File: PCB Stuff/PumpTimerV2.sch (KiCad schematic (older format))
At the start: 16 parts, among them J1 Conn_02x12_Odd_Even, J2 1935161, J3 282856-2, J4 282856-2, K1 ADW1205HLW, K2 ADW1205HLW, Q1 DMN67D7L, Q2 DMN67D7L

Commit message: Delete Altium files, add full Kicad project, update Kicad files
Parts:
- removed BT?: Battery_Cell, symbol Device:Battery_Cell
- removed C?: GMC31X5R107M10NT, Capacitor_SMD:C_1206_3216Metric_Pad1.33x1.80mm_HandSolder, symbol Device:C
- removed J3: 282856-2, TE_282856-2, symbol Connector:282856-2
- added BT1: 2032, Battery:BAT_HLD_2032, symbol Mechanical:Battery_Cell_Holder_2032
- added C1: 100u, Capacitor_SMD:C_1206_3216Metric_Pad1.33x1.80mm_HandSolder, symbol Device:C
- added J2: 282856-2, TE_282856-2, symbol Connector:282856-2
- added J5, J7: B6B-PH-SM4-TBT(LF)(SN), Connector_JST:JST_PH_B6B-PH-SM4-TB_1x06-1MP_P2.00mm_Vertical, symbol Connector_Generic:Conn_01x06
- added J6, J8: B4B-PH-SM4-TBT(LF)(SN), Connector_JST:JST_PH_B4B-PH-SM4-TB_1x04-1MP_P2.00mm_Vertical, symbol Connector_Generic:Conn_01x04
- added R1, R2: 1k, Resistor_SMD:R_0603_1608Metric_Pad0.98x0.95mm_HandSolder, symbol Device:R_US
- added R10, R11, R12, R5, R6, R7, R8, R9: 49.9, Resistor_SMD:R_0603_1608Metric_Pad0.98x0.95mm_HandSolder, symbol Device:R_US
- added R3, R4: 2k2, Resistor_SMD:R_0603_1608Metric_Pad0.98x0.95mm_HandSolder, symbol Device:R_US
- C2: renamed from C?; value GMC31X5R107M10NT -> 100u
- PS1: footprint CONV_RAC03-05SK -> power:RAC03-05SK
- U1: renamed from U?; footprint (none) -> Package_SO:SOP-14_127P780x200
- gave numbers to parts that had none: 1
- renumbered D2 to D3, J2 to J1, J4 to J3, J1 to J4
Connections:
- net labels added: RLY_R, RLY_S, RTC_~INT~
- net labels removed: GPIO14(Tx), GPIO15(Rx), GPIO17, GPIO18, GPIO4(CLK0)
- wire segments 70 -> 117
- no-connect marks 1 -> 4
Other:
- note added: "Expansion Ports\n (just in case)"
- note added: "Power Interface"
- note added: "Raspberry Pi Zero W Interface"
- note added: "Real-Time Clock"
- moved on the sheet: C2, D1, D2, D3, J1, J3, K1, K2, PS1, Q1, Q2, U1

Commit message: Adding button interface + LED indicator for manual switching of pump state
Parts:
- added D?: LED, symbol Device:LED
- added R?: R_US, symbol Device:R_US
- added R?: 2k2, Resistor_SMD:R_0603_1608Metric_Pad0.98x0.95mm_HandSolder, symbol Device:R_US
- added SW?: SW_Push, symbol Switch:SW_Push
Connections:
- net labels added: +3V3, ~BTN_RDY~
- wire segments 117 -> 127
- no-connect marks 4 -> 3
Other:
- moved on the sheet: U1

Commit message: Beginning layout. Removed a few non-critical components that will not fit.
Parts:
- removed J5, J7: B6B-PH-SM4-TBT(LF)(SN), Connector_JST:JST_PH_B6B-PH-SM4-TB_1x06-1MP_P2.00mm_Vertical, symbol Connector_Generic:Conn_01x06
- removed J8: B4B-PH-SM4-TBT(LF)(SN), Connector_JST:JST_PH_B4B-PH-SM4-TB_1x04-1MP_P2.00mm_Vertical, symbol Connector_Generic:Conn_01x04
- removed R12: 49.9, Resistor_SMD:R_0603_1608Metric_Pad0.98x0.95mm_HandSolder, symbol Device:R_US
- D4: renamed from D?; footprint (none) -> LED_SMD:LED_0603_1608Metric_Castellated; Part (none) -> SML-D12U1WT86
- R14: renamed from R?; value R_US -> 330; footprint (none) -> Resistor_SMD:R_0603_1608Metric_Pad0.98x0.95mm_HandSolder; Part (none) -> CRGCQ0603F330R
- SW1: renamed from SW?; value SW_Push -> TL3305AF160QG; footprint (none) -> Button_Switch_SMD:TL3305AF160QG; Part (none) -> TL3305AF160QG
- gave numbers to parts that had none: 1
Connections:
- wire segments 127 -> 108
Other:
- note added: "I2C Expansion Port\n (just in case)"
- note added: "NEED TO CHANGE TO CR1025"
- note added: "Override Button\n and Indicator"
- note removed: "Expansion Ports\n (just in case)"
- moved on the sheet: D1, D3, D4, J6, K1, K2, Q1, Q2, R1, R10, R11, R13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

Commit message: Same as last. Need to flip RPI and connector. Line up for mounting.
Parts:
- BT1: value 2032 -> 1632; footprint Battery:BAT_HLD_2032 -> temp:Vertical_16mm_coin; symbol Mechanical:Battery_Cell_Holder_2032 -> battery_cell:Battery_Cell
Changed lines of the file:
@@
 	9150 5500 9150 5550
 $Comp
-L Mechanical:Battery_Cell_Holder_2032 BT1
+L battery_cell:Battery_Cell BT1
 U 1 1 6076BE04
 P 9150 5400
 F 0 "BT1" H 9268 5496 50  0000 L CNN
-F 1 "2032" H 9268 5405 50  0000 L CNN
-F 2 "Battery:BAT_HLD_2032" V 9150 5460 50  0001 C CNN
+F 1 "1632" H 9268 5405 50  0000 L CNN
+F 2 "temp:Vertical_16mm_coin" V 9150 5460 50  0001 C CNN
 F 3 "~" V 9150 5460 50  0001 C CNN
 	1    9150 5400

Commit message: Clean-up, changing board size + adding bigger header for rpi
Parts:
- BT1: footprint temp:Vertical_16mm_coin -> Battery:Vertical_16mm_coin_holder; Part (none) -> Keystone 1069
- J4: value Conn_02x12_Odd_Even -> Conn_02x20_Odd_Even; footprint Connector_PinHeader_2.54mm:PinHeader_2x12_P2.54mm_Vertical -> Connector_PinHeader_2.54mm:PinHeader_2x20_P2.54mm_Vertical; symbol Connector_Generic:Conn_02x12_Odd_Even -> Connector_Generic:Conn_02x20_Odd_Even
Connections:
- no-connect marks 3 -> 19
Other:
- note removed: "NEED TO CHANGE TO CR1025"
- moved on the sheet: R10, R11, R3, R4, R5, R6, R7, R8, R9

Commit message: Routing and placement
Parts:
- removed R10, R11, R5, R6, R7, R8, R9: 49.9, Resistor_SMD:R_0603_1608Metric_Pad0.98x0.95mm_HandSolder, symbol Device:R_US
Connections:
- net +3V3: no longer R13.1
- net +5VD: now also R13.1
- net RLY_S: now also J4.8 (Pin_8); no longer J4.7 (Pin_7)
- net GPIO25: no longer names the net of J4.22 (Pin_22)
- net GPIO9(MISO): no longer names the net of J4.21 (Pin_21)
- no-connect marks 19 -> 28
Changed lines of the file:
@@
 Text Label 6150 2350 0    50   ~ 0
 RTC_~INT~
-Text Label 5550 2450 0    50   ~ 0
-GPIO27
-Text Label 5550 2550 0    50   ~ 0
-GPIO22
-NoConn ~ 6650 2650
-Wire Wire Line
-	6700 2650 6650 2650
-Text Label 5350 2750 0    50   ~ 0
-GPIO10(MOSI)
-Text Label 5350 2950 0    50   ~ 0
-GPIO11(SCLK)
 Wire Wire Line
 	6050 2250 6700 2250
 Wire Wire Line
 	6700 2350 6150 2350
-Wire Wire Line
-	6700 2850 6150 2850
 $Comp
 L power:GND #PWR023
@@
 	-1   0    0    1
 $EndComp
-Text Label 7800 2550 0    50   ~ 0
-GPIO23
-Text Label 7800 2650 0    50   ~ 0
-GPIO24
 $Comp
 L power:GND #PWR024
@@
 	-1   0    0    1
 $EndComp
-Text Label 7350 2850 0    50   ~ 0
-GPIO25
-Text Label 7750 2950 0    50   ~ 0
-GPIO8(SS0)
-Wire Wire Line
-	7200 2850 7350 2850
-Wire Wire Line
-	7350 2950 7200 2950
-Wire Wire Line
-	7200 2650 7350 2650
-Wire Wire Line
-	7200 2550 7350 2550
 $Comp
 L Diode:Generic_Diode D2
@@
 $EndComp
 $Comp
-L Device:R_US R7
-U 1 1 607C006A
-P 6050 2750
-F 0 "R7" V 5950 2650 50  0000 C CNN
-F 1 "49.9" V 6000 2900 50  0000 C CNN
-F 2 "Resistor_SMD:R_0603_1608Metric_Pad0.98x0.95mm_HandSolder" V 6090 2740 50  0001 C CNN
-F 3 "ERJ-3EKF49R9V" H 6050 2750 50  0001 C CNN
-	1    6050 2750
-	0    1    1    0
-$EndComp
-Text Label 6150 2850 0    50   ~ 0
-GPIO9(MISO)
-Wire Wire Line
-	5900 2950 5350 2950
-Wire Wire Line
-	5350 2750 5900 2750
-Wire Wire Line
-	6200 2750 6700 2750
-Wire Wire Line
-	6700 2950 6200 2950
-$Comp
-L Device:R_US R11
-U 1 1 607CC497
-P 7500 2950
-F 0 "R11" V 7450 2800 50  0000 C CNN
-F 1 "49.9" V 7600 2950 50  0000 C CNN
-F 2 "Resistor_SMD:R_0603_1608Metric_Pad0.98x0.95mm_HandSolder" V 7540 2940 50  0001 C CNN
-F 3 "ERJ-3EKF49R9V" H 7500 2950 50  0001 C CNN
-	1    7500 2950
-	0    1    1    0
-$EndComp
-Wire Wire Line
-	7650 2950 7750 2950
-$Comp
-L Device:R_US R8
-U 1 1 607D7BAE
-P 6050 2950
-F 0 "R8" V 6100 2800 50  0000 C CNN
-F 1 "49.9" V 6100 3150 50  0000 C CNN
-F 2 "Resistor_SMD:R_0603_1608Metric_Pad0.98x0.95mm_HandSolder" V 6090 2940 50  0001 C CNN
-F 3 "ERJ-3EKF49R9V" H 6050 2950 50  0001 C CNN
-	1    6050 2950
-	0    1    1    0
-$EndComp
-$Comp
 L Device:C C1
 U 1 1 607DE07A
@@
 	-1   0    0    1
 $EndComp
-$Comp
-L Device:R_US R9
-U 1 1 607F57A6
-P 7500 2550
-F 0 "R9" V 7450 2400 50  0000 C CNN
-F 1 "49.9" V 7450 2700 50  0000 C CNN
-F 2 "Resistor_SMD:R_0603_1608Metric_Pad0.98x0.95mm_HandSolder" V 7540 2540 50  0001 C CNN
-F 3 "ERJ-3EKF49R9V" H 7500 2550 50  0001 C CNN
-	1    7500 2550
-	0    1    1    0
-$EndComp
-$Comp
-L Device:R_US R10
-U 1 1 607F6412
-P 7500 2650
-F 0 "R10" V 7450 2500 50  0000 C CNN
-F 1 "49.9" V 7450 2800 50  0000 C CNN
-F 2 "Resistor_SMD:R_0603_1608Metric_Pad0.98x0.95mm_HandSolder" V 7540 2640 50  0001 C CNN
-F 3 "ERJ-3EKF49R9V" H 7500 2650 50  0001 C CNN
-	1    7500 2650
-	0    1    1    0
-$EndComp
-Wire Wire Line
-	7650 2650 7800 2650
-Wire Wire Line
-	7650 2550 7800 2550
 Wire Wire Line
 	7200 2450 8150 2450
@@
 	9000 1750 9550 1750
 $Comp
-L Device:R_US R5
-U 1 1 60879D01
-P 6050 2450
-F 0 "R5" V 6000 2300 50  0000 C CNN
-F 1 "49.9" V 6000 2600 50  0000 C CNN
-F 2 "Resistor_SMD:R_0603_1608Metric_Pad0.98x0.95mm_HandSolder" V 6090 2440 50  0001 C CNN
-F 3 "ERJ-3EKF49R9V" H 6050 2450 50  0001 C CNN
-	1    6050 2450
-	0    1    1    0
-$EndComp
-$Comp
-L Device:R_US R6
-U 1 1 6087A462
-P 6050 2550
-F 0 "R6" V 6000 2400 50  0000 C CNN
-F 1 "49.9" V 6000 2700 50  0000 C CNN
-F 2 "Resistor_SMD:R_0603_1608Metric_Pad0.98x0.95mm_HandSolder" V 6090 2540 50  0001 C CNN
-F 3 "ERJ-3EKF49R9V" H 6050 2550 50  0001 C CNN
-	1    6050 2550
-	0    1    1    0
-$EndComp
-Wire Wire Line
-	5550 2550 5900 2550
-Wire Wire Line
-	5900 2450 5550 2450
-Wire Wire Line
-	6200 2450 6700 2450
-Wire Wire Line
-	6700 2550 6200 2550
-$Comp
 L power:GND #PWR035
 U 1 1 6088F768
@@
 	1    0    0    -1
 $EndComp
-NoConn ~ 7200 2150
 Text Notes 9300 1200 0    79   ~ 0
 I2C Expansion Port\n   (just in case)
@@
 Wire Wire Line
 	2000 6750 2300 6750
-Text Label 6150 2150 0    50   ~ 0
+Text Label 7800 2150 0    50   ~ 0
 RLY_S
-Wire Wire Line
-	6150 2150 6700 2150
-Text Label 7800 2350 0    50   ~ 0
-RLY_R
-Wire Wire Line
-	7800 2350 7200 2350
 Text Label 2000 6750 0    50   ~ 0
 RLY_S
@@
 F 3 "" H 10800 3300 50  0001 C CNN
 	1    10800 3300
-	1    0    0    -1
-$EndComp
-$Comp
-L power:+3V3 #PWR0103
-U 1 1 60797B23
-P 8900 2900
-F 0 "#PWR0103" H 8900 2750 50  0001 C CNN
-F 1 "+3V3" H 8915 3073 50  0000 C CNN
-F 2 "" H 8900 2900 50  0001 C CNN
-F 3 "" H 8900 2900 50  0001 C CNN
-	1    8900 2900
 	1    0    0    -1
 $EndComp
@@
 NoConn ~ 7200 3050
 NoConn ~ 7200 3450
+$Comp
+L power:+5VD #PWR0103
+U 1 1 607FB41A
+P 8900 2900
+F 0 "#PWR0103" H 8900 2750 50  0001 C CNN
+F 1 "+5VD" H 8915 3073 50  0000 C CNN
+F 2 "" H 8900 2900 50  0001 C CNN
+F 3 "" H 8900 2900 50  0001 C CNN
+	1    8900 2900
+	1    0    0    -1
+$EndComp
+Wire Wire Line
+	7800 2350 7200 2350
+Text Label 7800 2350 0    50   ~ 0
+RLY_R
+Wire Wire Line
+	7200 2150 7800 2150
+NoConn ~ 6700 2150
+NoConn ~ 7200 2550
+NoConn ~ 7200 2650
+NoConn ~ 7200 2950
+NoConn ~ 7200 2850
+NoConn ~ 6700 2450
+NoConn ~ 6700 2550
+NoConn ~ 6700 2750
+NoConn ~ 6700 2850
+NoConn ~ 6700 2950
+NoConn ~ 6700 2650
 $EndSCHEMATC

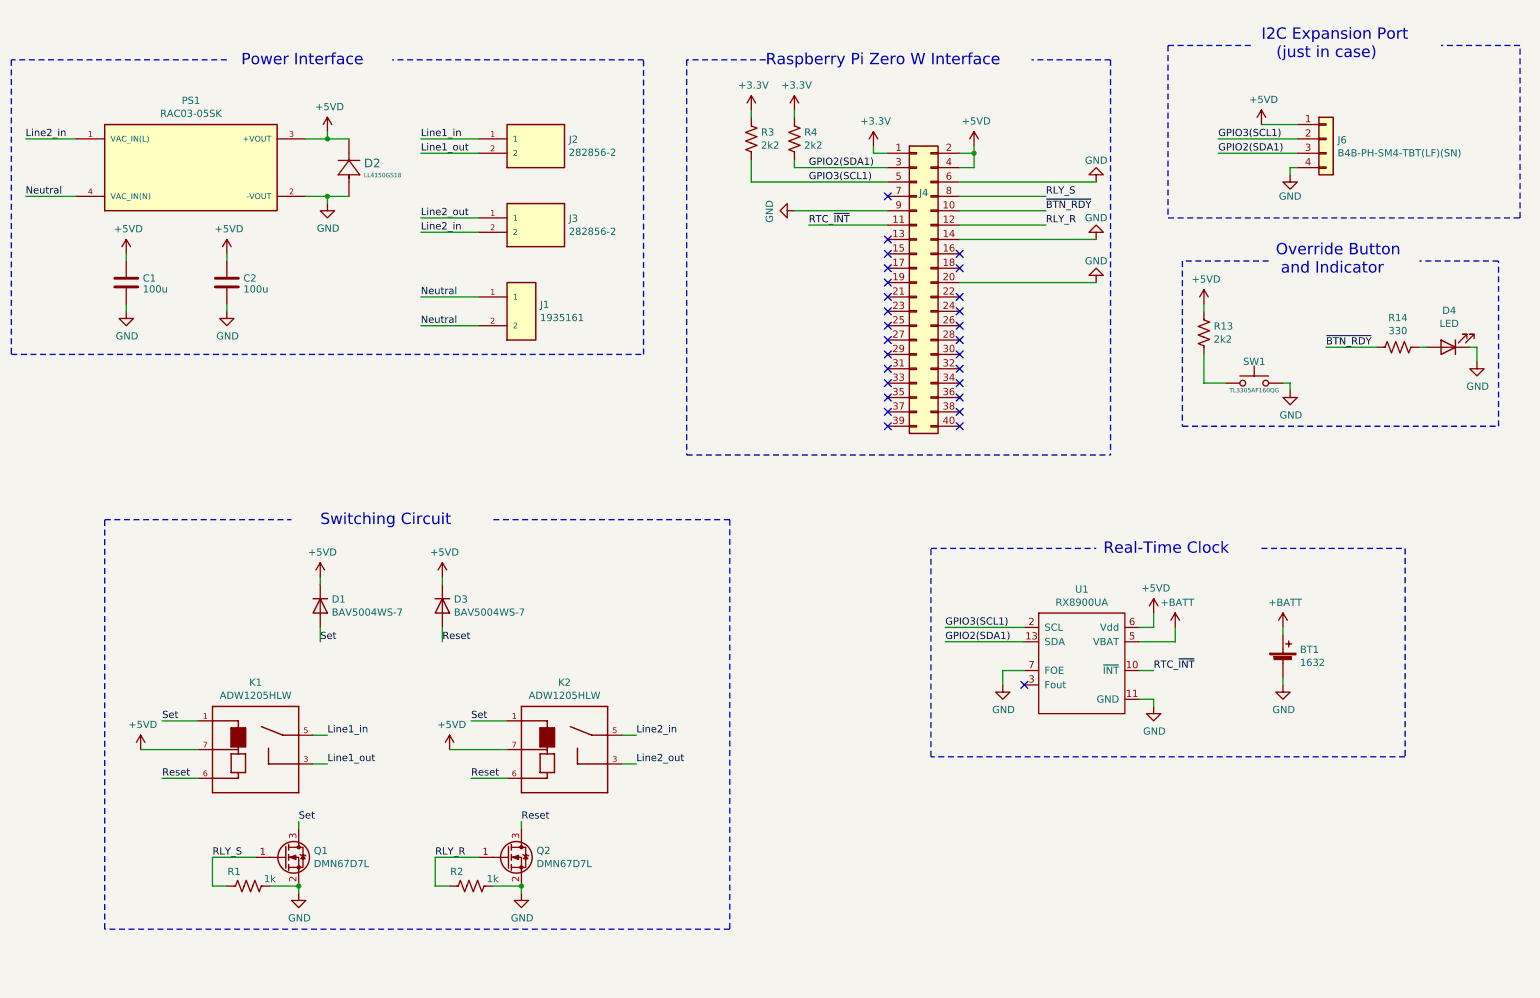
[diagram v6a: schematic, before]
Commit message: Slight rearranging, changing neutral screw terminal to higher-current model
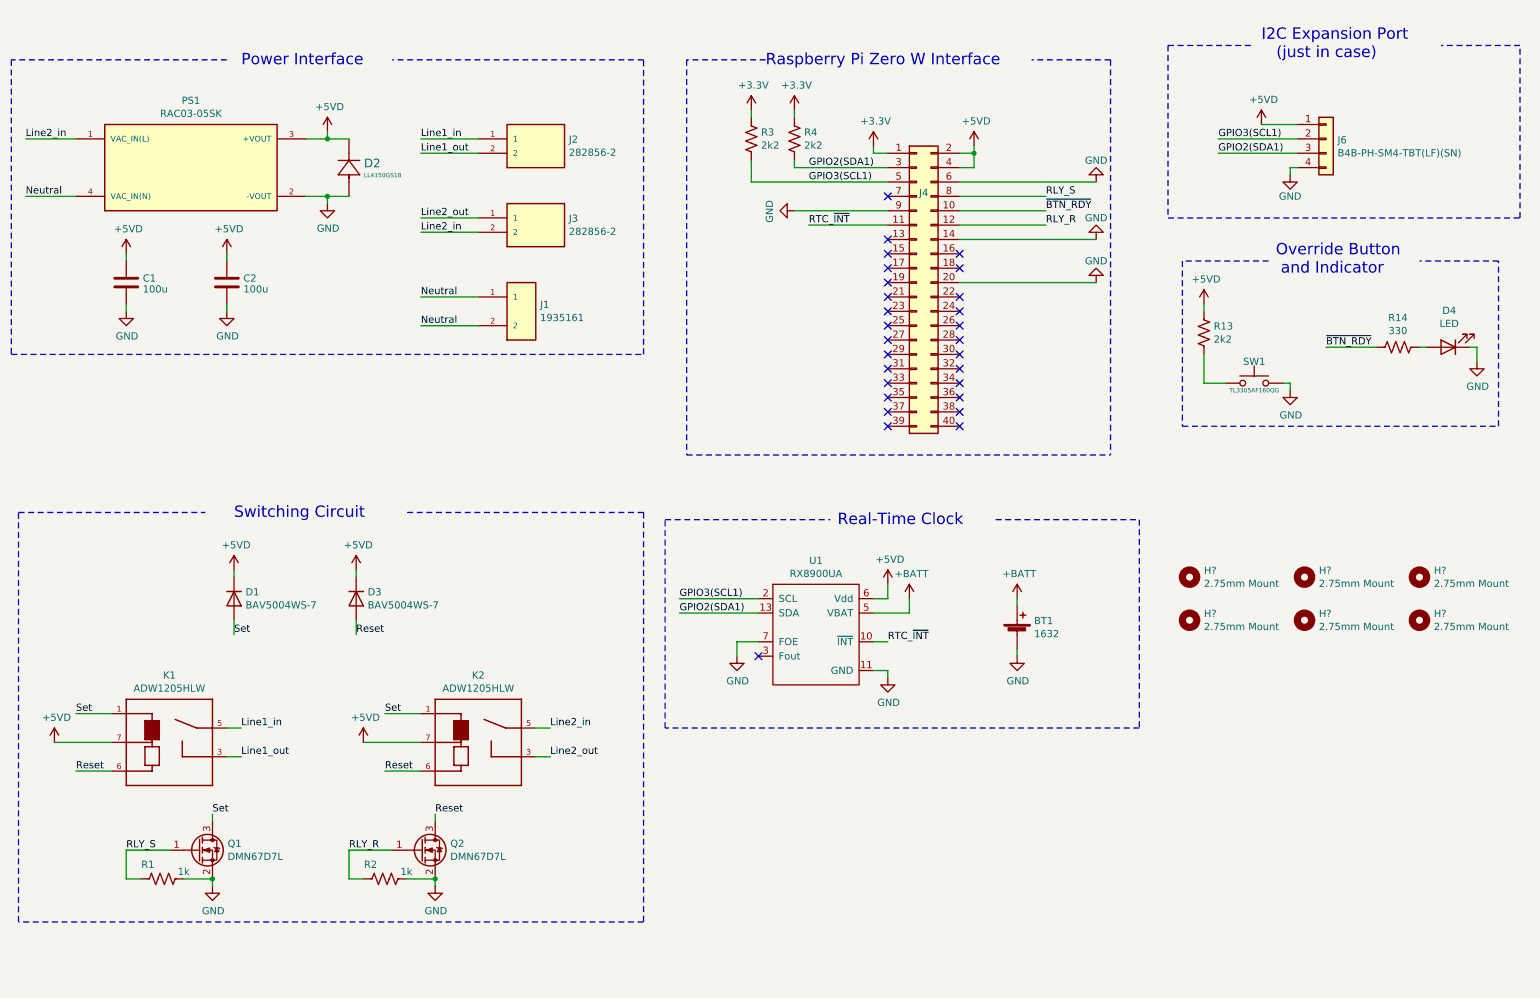
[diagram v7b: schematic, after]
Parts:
- added H? (x6): 2.75mm Mount, MountingHole:MountingHole_2.7mm_M2.5, symbol Mechanical:MountingHole
- J4: Mating (none) -> PPTC202LFBN-RC; Part (none) -> M20-9982046
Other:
- moved on the sheet: BT1, D1, D3, K1, K2, Q1, Q2, R1, R2, U1
